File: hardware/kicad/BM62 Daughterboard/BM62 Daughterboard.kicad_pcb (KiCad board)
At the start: 2 copper layers, 29 x 34.5 mm, 10 parts, among them J1 Conn_2x4, SW1 SW_DIP_x03, U1 BM62

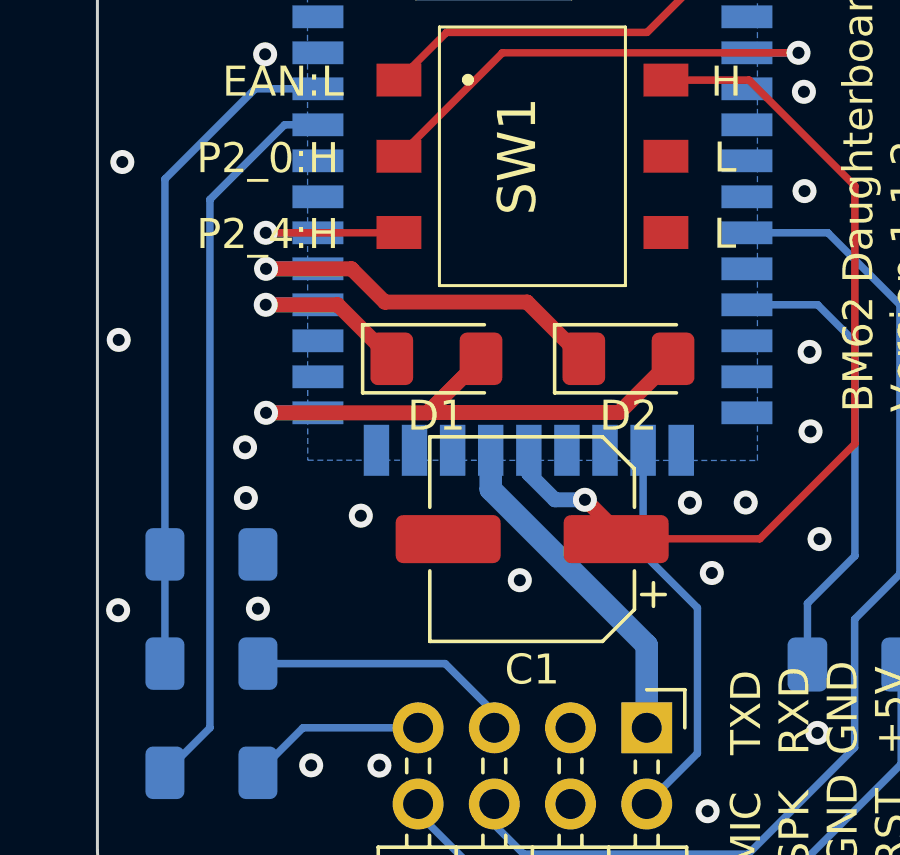
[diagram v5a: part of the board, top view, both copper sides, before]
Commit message: Clean up BM62 Daughterboard KiCad project
* Use generalized names for project-level symbol/footprint/model libraries.
* Remove a 3D model that belongs in the SymacSys_Parts library.
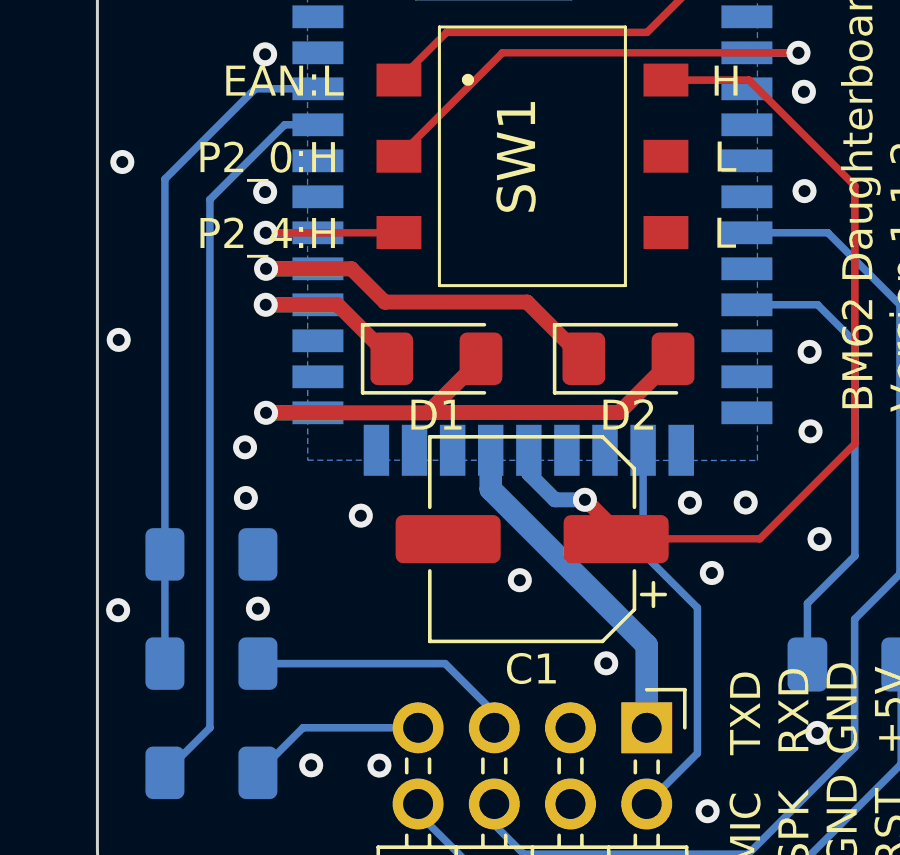
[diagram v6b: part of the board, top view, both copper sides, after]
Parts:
- U1: footprint BM62 Daughterboard:Microchip BM62 -> Project Footprints:Microchip BM62
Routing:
- net GND: vias 31 -> 33
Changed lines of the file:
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@@
         (effects (font (size 1.27 1.27) (thickness 0.254)))
     )
-    (fp_text value "SW_DIP_x03" (at 0 0.5 90) (layer "F.SilkS") hide
+    (fp_text value "SW_DIP_x03" (at 0 0.5 90) (layer "F.Fab") hide
         (effects (font (size 1.27 1.27) (thickness 0.254)))
     )
@@
     (pad "6" smd rect (at -2.54 -4.45 270) (size 1.1 1.5) (layers "F.Cu" "F.Paste" "F.Mask")
       (net 4 "/VDD_IO") (pintype "passive"))
-    (model "${KIPRJMOD}/BM62 Daughterboard.3dshapes/CUI_DEVICES_DS04-254-1-03BK-SMT.step"
+    (model "D:/SamacSys_PCB_Library/KiCad/SamacSys_Parts.3dshapes/CUI_DEVICES_DS04-254-1-03BK-SMT.step"
       (offset (xyz -4 9 0.9))
       (scale (xyz 1 1 1))
@@
     )
   )
-  (footprint "BM62 Daughterboard:Microchip BM62" (layer "B.Cu")
+  (footprint "Project Footprints:Microchip BM62" (layer "B.Cu")
     (at 155 104 180)
     (property "JLCPCB Part#" "C610451")
@@
     (property "Sheetname" "")
     (attr through_hole)
-    (fp_text reference "U1" (at 8.03 3.93) (layer "B.SilkS")
-        (effects (font (size 1 1) (thickness 0.15)) (justify mirror))
-    )
-    (fp_text value "BM62" (at 7.92 2.565) (layer "B.SilkS")
-        (effects (font (size 1 1) (thickness 0.15)) (justify mirror))
+    (fp_text reference "U1" (at 7.75 8.95) (layer "B.SilkS")
+        (effects (font (size 1 1) (thickness 0.15)) (justify mirror))
+    )
+    (fp_text value "BM62" (at 7.65 11) (layer "B.Fab")
+        (effects (font (size 1 1) (thickness 0.15)) (justify mirror))
+    )
+    (fp_text user "${REFERENCE}" (at 7.6 7.3) (layer "B.Fab")
+        (effects (font (size 1 1) (thickness 0.1)) (justify mirror))
     )
     (fp_line (start 0 0) (end 2 0)
@@
         (pts
           (xy 153.8 86.4)
-          (xy 155 86.4)
-          (xy 155 85)
-          (xy 140 85)
-          (xy 140 86.4)
+          (xy 155.5 86.4)
+          (xy 155.5 85)
+          (xy 139.5 85)
+          (xy 139.5 86.4)
           (xy 141.2 86.4)
           (xy 141.2 102.8)
-          (xy 140 102.8)
-          (xy 140 104)
-          (xy 141.8 104)
+          (xy 139.5 102.8)
+          (xy 139.5 104.5)
+          (xy 141.8 104.5)
           (xy 141.8 102.8)
           (xy 152.9 102.8)
-          (xy 152.9 104)
-          (xy 155 104)
-          (xy 155 102.8)
+          (xy 152.9 104.5)
+          (xy 155.5 104.5)
+          (xy 155.5 102.8)
           (xy 153.8 102.8)
         )
       )
     )
-    (model "${KIPRJMOD}/BM62 Daughterboard.3dshapes/BM62SPKA1MC2-0001AA--3DModel-STEP-56544.STEP"
+    (model "${KIPRJMOD}/Project Models.3dshapes/BM62SPKA1MC2-0001AA--3DModel-STEP-56544.STEP"
       (offset (xyz 7.5 14.5 0))
       (scale (xyz 1 1 1))
@@
   (segment (start 139.85 112.9) (end 143.69 112.9) (width 0.25) (layer "B.Cu") (net 2))
   (segment (start 138.35 114.4) (end 139.85 112.9) (width 0.25) (layer "B.Cu") (net 2))
+  (via (at 149.96 110.75) (size 0.8) (drill 0.4) (layers "F.Cu" "B.Cu") (free) (net 3))
   (via (at 133.69 108.98) (size 0.8) (drill 0.4) (layers "F.Cu" "B.Cu") (free) (net 3))
   (via (at 152.75 105.4) (size 0.8) (drill 0.4) (layers "F.Cu" "B.Cu") (free) (net 3))
@@
   (via (at 156.57 95.01) (size 0.8) (drill 0.4) (layers "F.Cu" "B.Cu") (free) (net 3))
   (via (at 156.55 91.7) (size 0.8) (drill 0.4) (layers "F.Cu" "B.Cu") (free) (net 3))
+  (via (at 138.59 95.04) (size 0.8) (drill 0.4) (layers "F.Cu" "B.Cu") (free) (net 3))
   (via (at 138.59 90.45) (size 0.8) (drill 0.4) (layers "F.Cu" "B.Cu") (free) (net 3))
   (via (at 147.08 107.98) (size 0.8) (drill 0.4) (layers "F.Cu" "B.Cu") (free) (net 3))
@@
   (segment (start 158.25 103.43) (end 158.25 94.84) (width 0.25) (layer "F.Cu") (net 4))
   (via (at 149.25 105.3) (size 0.8) (drill 0.4) (layers "F.Cu" "B.Cu") (net 4))
+  (segment (start 147.38 104.43) (end 148.25 105.3) (width 0.5) (layer "B.Cu") (net 4))
+  (segment (start 147.38 103.65) (end 147.38 104.43) (width 0.5) (layer "B.Cu") (net 4))
   (segment (start 148.25 105.3) (end 149.25 105.3) (width 0.5) (layer "B.Cu") (net 4))
-  (segment (start 147.38 103.64) (end 147.38 104.43) (width 0.5) (layer "B.Cu") (net 4))
-  (segment (start 147.38 104.43) (end 148.25 105.3) (width 0.5) (layer "B.Cu") (net 4))
   (segment (start 158.25 100.04) (end 157.01 98.8) (width 0.25) (layer "B.Cu") (net 25))
   (segment (start 157.01 98.8) (end 154.66 98.8) (width 0.25) (layer "B.Cu") (net 25))
@@
   (segment (start 140.34 102.4) (end 138.64 102.4) (width 0.5) (layer "B.Cu") (net 27))
   (segment (start 140.35 102.39) (end 140.34 102.4) (width 0.5) (layer "B.Cu") (net 27))
-  (segment (start 146.11 104.95) (end 146.11 103.64) (width 0.75) (layer "B.Cu") (net 28))
+  (segment (start 146.11 104.95) (end 146.11 103.65) (width 0.75) (layer "B.Cu") (net 28))
   (segment (start 151.31 110.15) (end 146.11 104.95) (width 0.75) (layer "B.Cu") (net 28))
   (segment (start 151.31 112.9) (end 151.31 110.15) (width 0.75) (layer "B.Cu") (net 28))
@@
   (segment (start 138.62 97.6) (end 140.35 97.6) (width 0.5) (layer "B.Cu") (net 29))
   (segment (start 151.31 115.44) (end 153 113.75) (width 0.25) (layer "B.Cu") (net 30))
+  (segment (start 151.19 107.09) (end 151.19 103.65) (width 0.25) (layer "B.Cu") (net 30))
   (segment (start 153 113.75) (end 153 108.9) (width 0.25) (layer "B.Cu") (net 30))
-  (segment (start 151.19 107.09) (end 151.19 103.64) (width 0.25) (layer "B.Cu") (net 30))
   (segment (start 153 108.9) (end 151.19 107.09) (width 0.25) (layer "B.Cu") (net 30))
   (segment (start 157.35 96.4) (end 154.66 96.4) (width 0.25) (layer "B.Cu") (net 31))
